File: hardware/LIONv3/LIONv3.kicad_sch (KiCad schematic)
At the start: 31 parts, among them SW1 RESET, SW2 BOOT, U14 HC-1_25-2PWT, U15 HC-1_25-2PWT, U19 HC-1_25-2PWT, U2 TYPE-C_16PIN_2MD(073), U21 USBLC6-2SC6, U3 ESP32-C6-MINI-1-N4, U4 TMP112AIDRLR, U9 HC-1_25-2PWT

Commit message: feat(hardware): add pre-review schematic
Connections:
- net +4.4V renamed +4.69V
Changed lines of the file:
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@@
+	)
+	(symbol
+		(lib_id "power:+5V")
+		(at 113.03 166.37 0)
+		(unit 1)
+		(body_style 1)
+		(exclude_from_sim no)
+		(in_bom yes)
+		(on_board yes)
+		(in_pos_files yes)
+		(dnp no)
+		(fields_autoplaced yes)
+		(property "Reference" "#PWR046"
+			(at 113.03 170.18 0)
+			(hide yes)
+			(show_name no)
+			(do_not_autoplace no)
+			(effects
+				(font
+					(size 1.27 1.27)
+				)
+			)
+		)
+		(property "Value" "+4.69V"
+			(at 113.03 161.29 0)
+			(show_name no)
+			(do_not_autoplace yes)
+			(effects
+				(font
+					(size 1.27 1.27)
+				)
+			)
+		)
+		(property "Footprint" ""
+			(at 113.03 166.37 0)
+			(hide yes)
+			(show_name no)
+			(do_not_autoplace no)
+			(effects
+				(font
+					(size 1.27 1.27)
+				)
+			)
+		)
+		(property "Datasheet" ""
+			(at 113.03 166.37 0)
+			(hide yes)
+			(show_name no)
+			(do_not_autoplace no)
+			(effects
+				(font
+					(size 1.27 1.27)
+				)
+			)
+		)
+		(property "Description" "Power symbol creates a global label with name \"+5V\""
+			(at 113.03 166.37 0)
+			(hide yes)
+			(show_name no)
+			(do_not_autoplace no)
+			(effects
+				(font
+					(size 1.27 1.27)
+				)
+			)
+		)
+		(pin "1"
+		)
+		(instances
+			(project "LIONv3"
+				(path "/3cc9e06f-00d0-4bec-822f-2e156022ced4"
+					(reference "#PWR046")
+					(unit 1)
+				)
+			)
+		)
 	)
 	(symbol
@@
 					(unit 1)
 				)
-			)
-		)
-	)
-	(symbol
-		(lib_id "power:+5V")
-		(at 113.03 166.37 0)
-		(unit 1)
-		(body_style 1)
-		(exclude_from_sim no)
-		(in_bom yes)
-		(on_board yes)
-		(in_pos_files yes)
-		(dnp no)
-		(fields_autoplaced yes)
-		(property "Reference" "#PWR046"
-			(at 113.03 170.18 0)
-			(hide yes)
-			(show_name no)
-			(do_not_autoplace no)
-			(effects
-				(font
-					(size 1.27 1.27)
-				)
-			)
-		)
-		(property "Value" "+4.4V"
-			(at 113.03 161.29 0)
-			(show_name no)
-			(do_not_autoplace no)
-			(effects
-				(font
-					(size 1.27 1.27)
-				)
-			)
-		)
-		(property "Footprint" ""
-			(at 113.03 166.37 0)
-			(hide yes)
-			(show_name no)
-			(do_not_autoplace no)
-			(effects
-				(font
-					(size 1.27 1.27)
-				)
-			)
-		)
-		(property "Datasheet" ""
-			(at 113.03 166.37 0)
-			(hide yes)
-			(show_name no)
-			(do_not_autoplace no)
-			(effects
-				(font
-					(size 1.27 1.27)
-				)
-			)
-		)
-		(property "Description" "Power symbol creates a global label with name \"+5V\""
-			(at 113.03 166.37 0)
-			(hide yes)
-			(show_name no)
-			(do_not_autoplace no)
-			(effects
-				(font
-					(size 1.27 1.27)
-				)
-			)
-		)
-		(pin "1"
-		)
-		(instances
-			(project "LIONv3"
-				(path "/3cc9e06f-00d0-4bec-822f-2e156022ced4"
-					(reference "#PWR046")
-					(unit 1)
-				)

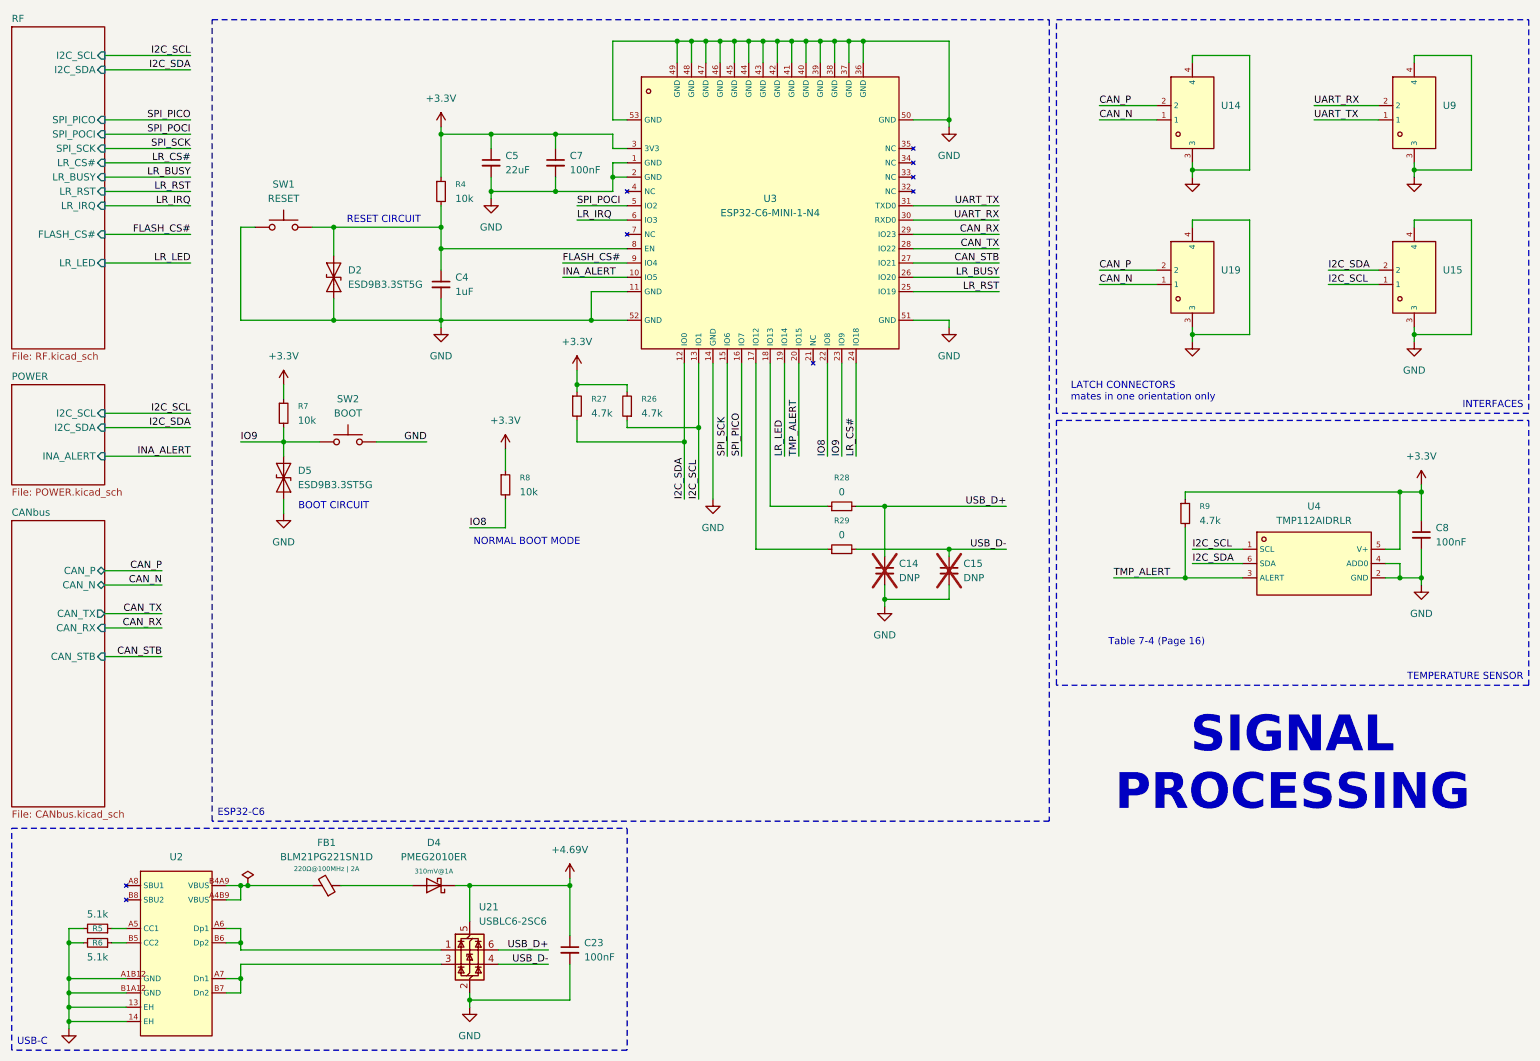
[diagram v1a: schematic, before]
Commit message: feat(hardware): add TestPoints
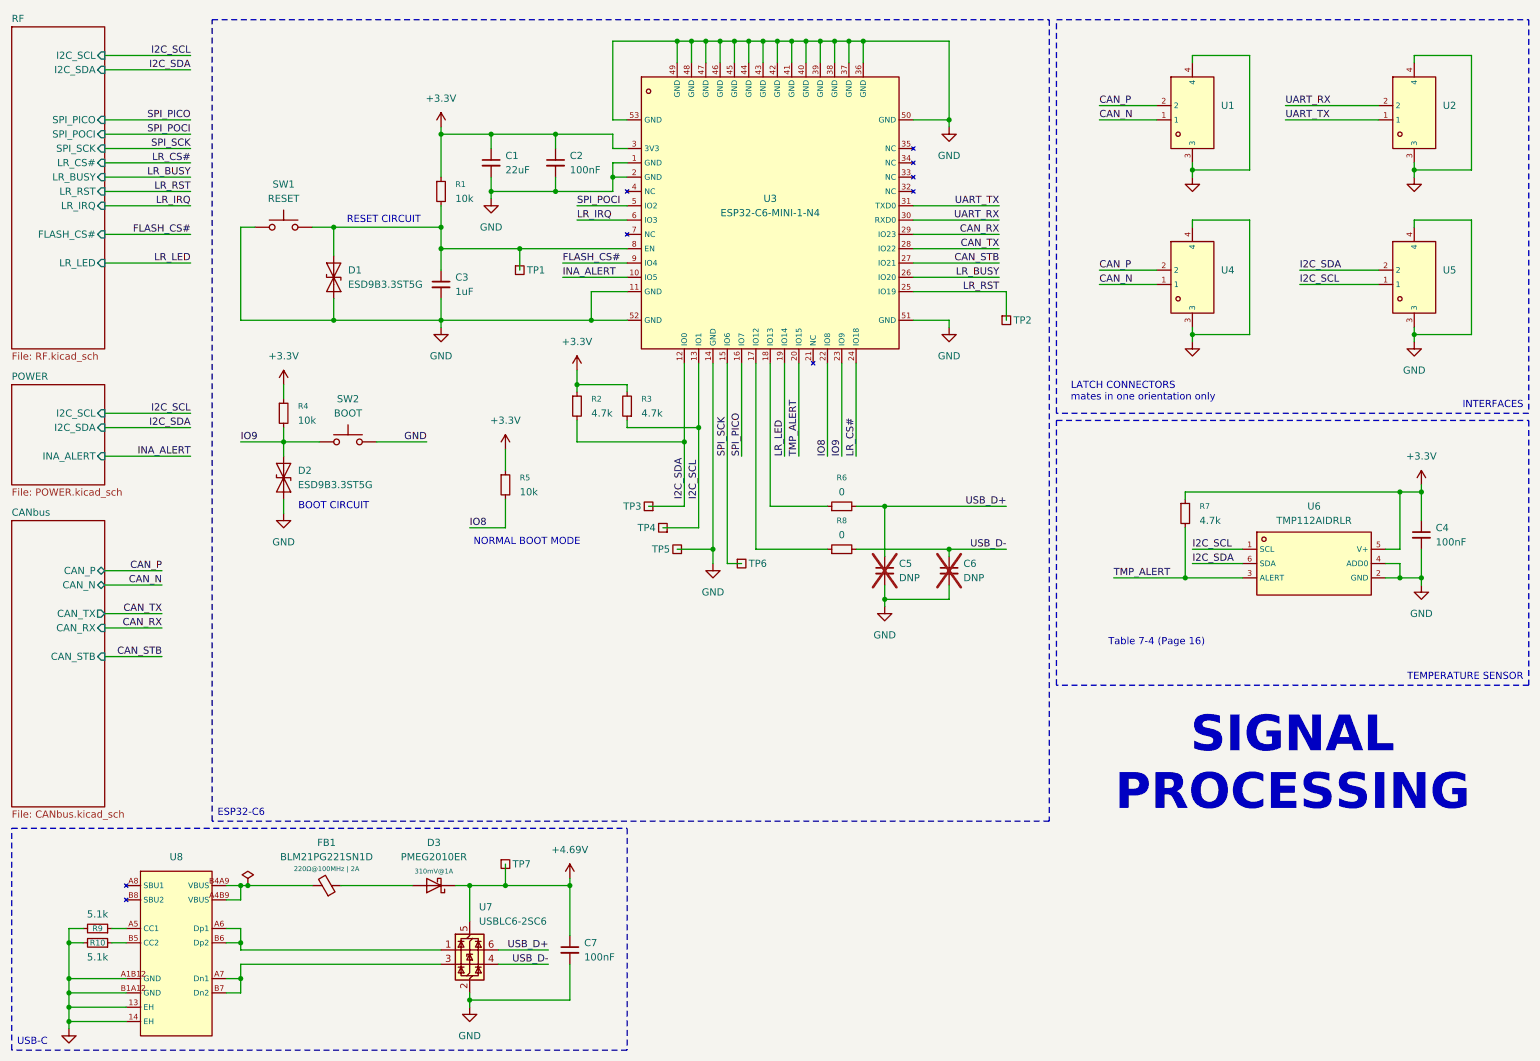
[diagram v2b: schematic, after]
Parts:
- added TP1, TP2, TP3, TP4, TP5, TP6, TP7: TestPoint_Square, TestPoint:TestPoint_Pad_D1.5mm, symbol Connector:TestPoint_Square
- renumbered C5 to C1, C7 to C2, C4 to C3, C8 to C4, C14 to C5, C15 to C6, C23 to C7, D2 to D1, D5 to D2, D4 to D3, R4 to R1, R6 to R10, R27 to R2, R26 to R3, R7 to R4, R8 to R5, R28 to R6, R9 to R7, R29 to R8, R5 to R9, U14 to U1, U9 to U2, U19 to U4, U15 to U5, U4 to U6, U21 to U7, U2 to U8
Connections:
- net +4.69V: now also TP7.1
- net GND: now also TP5.1
- net I2C_SCL: now also TP4.1
- net I2C_SDA: now also TP3.1
- net LR_RST: now also TP2.1
- net SPI_SCK: now also TP6.1
- net at C3.1, D1.2 (A2), R1.2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: now also TP1.1

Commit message: feat(hardware): start PCB design
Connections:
- net D+: now reaches U7.1 (I/O1), U8.A6 (Dp1), U8.B6 (Dp2)
- net D-: now reaches U7.3 (I/O2), U8.A7 (Dn1), U8.B7 (Dn2)
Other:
- moved on the sheet: SW1
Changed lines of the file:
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@@
 	(text "RESET CIRCUIT"
 		(exclude_from_sim no)
-		(at 80.01 49.53 0)
+		(at 80.01 50.8 0)
 		(effects
 			(font
@@
 	)
 	(junction
-		(at 90.17 50.8)
-		(diameter 0)
-		(color 0 0 0 0)
-	)
-	(junction
 		(at 110.49 34.29)
 		(diameter 0)
@@
 	)
 	(junction
+		(at 90.17 52.07)
+		(diameter 0)
+		(color 0 0 0 0)
+	)
+	(junction
 		(at 147.32 17.78)
 		(diameter 0)
@@
 	)
 	(junction
-		(at 71.12 50.8)
-		(diameter 0)
-		(color 0 0 0 0)
-	)
-	(junction
 		(at 262.89 69.85)
 		(diameter 0)
@@
 	)
 	(junction
-		(at 71.12 67.31)
+		(at 110.49 44.45)
 		(diameter 0)
 		(color 0 0 0 0)
 	)
 	(junction
-		(at 110.49 44.45)
+		(at 160.02 17.78)
 		(diameter 0)
 		(color 0 0 0 0)
 	)
 	(junction
-		(at 160.02 17.78)
+		(at 71.12 67.31)
 		(diameter 0)
 		(color 0 0 0 0)
@@
 	)
 	(junction
+		(at 71.12 52.07)
+		(diameter 0)
+		(color 0 0 0 0)
+	)
+	(junction
 		(at 168.91 100.33)
 		(diameter 0)
@@
 	(wire
 		(pts
-			(xy 90.17 46.99) (xy 90.17 50.8)
-		)
-		(stroke
-			(width 0)
-			(type default)
-		)
-	)
-	(wire
-		(pts
 			(xy 90.17 63.5) (xy 90.17 67.31)
 		)
@@
 	(wire
 		(pts
-			(xy 54.61 50.8) (xy 57.15 50.8)
+			(xy 54.61 52.07) (xy 57.15 52.07)
+		)
+		(stroke
+			(width 0)
+			(type default)
+		)
+	)
+	(wire
+		(pts
+			(xy 90.17 46.99) (xy 90.17 52.07)
 		)
 		(stroke
@@
 	(wire
 		(pts
-			(xy 30.48 111.76) (xy 40.64 111.76)
+			(xy 30.48 111.76) (xy 45.72 111.76)
 		)
 		(stroke
@@
 	(wire
 		(pts
-			(xy 30.48 127) (xy 40.64 127)
+			(xy 30.48 127) (xy 45.72 127)
 		)
 		(stroke
@@
 	(wire
 		(pts
-			(xy 54.61 50.8) (xy 54.61 67.31)
+			(xy 54.61 52.07) (xy 54.61 67.31)
 		)
 		(stroke
@@
 	(wire
 		(pts
+			(xy 90.17 52.07) (xy 90.17 54.61)
+		)
+		(stroke
+			(width 0)
+			(type default)
+		)
+	)
+	(wire
+		(pts
 			(xy 30.48 86.36) (xy 45.72 86.36)
 		)
@@
 	(wire
 		(pts
-			(xy 30.48 121.92) (xy 40.64 121.92)
+			(xy 30.48 121.92) (xy 45.72 121.92)
 		)
 		(stroke
@@
 	(wire
 		(pts
-			(xy 71.12 50.8) (xy 90.17 50.8)
+			(xy 71.12 52.07) (xy 90.17 52.07)
 		)
 		(stroke
@@
 	(wire
 		(pts
-			(xy 67.31 50.8) (xy 71.12 50.8)
+			(xy 67.31 52.07) (xy 71.12 52.07)
 		)
 		(stroke
@@
 	(wire
 		(pts
-			(xy 30.48 114.3) (xy 40.64 114.3)
+			(xy 30.48 114.3) (xy 45.72 114.3)
 		)
 		(stroke
@@
 	(wire
 		(pts
-			(xy 71.12 50.8) (xy 71.12 55.88)
-		)
-		(stroke
-			(width 0)
-			(type default)
-		)
-	)
-	(wire
-		(pts
 			(xy 158.75 107.95) (xy 146.05 107.95)
 		)
@@
 	(wire
 		(pts
-			(xy 90.17 50.8) (xy 90.17 54.61)
-		)
-		(stroke
-			(width 0)
-			(type default)
-		)
-	)
-	(wire
-		(pts
 			(xy 127 100.33) (xy 133.35 100.33)
 		)
@@
 	(wire
 		(pts
-			(xy 30.48 119.38) (xy 40.64 119.38)
+			(xy 30.48 119.38) (xy 45.72 119.38)
 		)
 		(stroke
@@
 	(wire
 		(pts
+			(xy 71.12 52.07) (xy 71.12 55.88)
+		)
+		(stroke
+			(width 0)
+			(type default)
+		)
+	)
+	(wire
+		(pts
 			(xy 114.3 88.9) (xy 114.3 85.09)
 		)
@@
 	)
 	(label "CAN_N"
-		(at 40.64 114.3 180)
+		(at 45.72 114.3 180)
 		(effects
 			(font
@@
 	)
 	(label "CAN_STB"
-		(at 40.64 127 180)
+		(at 45.72 127 180)
 		(effects
 			(font
@@
 		)
 	)
+	(label "D-"
+		(at 73.66 181.61 0)
+		(effects
+			(font
+				(size 1.27 1.27)
+			)
+			(justify left bottom)
+		)
+	)
 	(label "UART_TX"
 		(at 189.23 46.99 180)
@@
 	)
 	(label "CAN_TX"
-		(at 40.64 119.38 180)
+		(at 45.72 119.38 180)
 		(effects
 			(font
@@
 	)
 	(label "CAN_P"
-		(at 40.64 111.76 180)
+		(at 45.72 111.76 180)
 		(effects
 			(font
@@
 	)
 	(label "CAN_RX"
-		(at 40.64 121.92 180)
+		(at 45.72 121.92 180)
 		(effects
 			(font
@@
 		)
 	)
+	(label "D+"
+		(at 73.66 179.07 0)
+		(effects
+			(font
+				(size 1.27 1.27)
+			)
+			(justify left bottom)
+		)
+	)
 	(symbol
 		(lib_id "power:+5V")
@@
 	(symbol
 		(lib_id "Switch:SW_Push")
-		(at 62.23 50.8 0)
+		(at 62.23 52.07 0)
 		(unit 1)
 		(body_style 1)
@@
 		(fields_autoplaced yes)
 		(property "Reference" "SW1"
-			(at 62.23 43.18 0)
+			(at 62.23 44.45 0)
 			(show_name no)
 			(do_not_autoplace no)
@@
 		)
 		(property "Value" "RESET"
-			(at 62.23 45.72 0)
+			(at 62.23 46.99 0)
 			(show_name no)
 			(do_not_autoplace no)
@@
 		)
 		(property "Footprint" "LIONv3-Footprints:KEY-SMD_L3.9-W3.0-LS5.0"
-			(at 62.23 45.72 0)
+			(at 62.23 46.99 0)
 			(hide yes)
 			(show_name no)
@@
 		)
 		(property "Datasheet" ""
-			(at 62.23 45.72 0)
+			(at 62.23 46.99 0)
 			(hide yes)
 			(show_name no)
@@
 		)
 		(property "Description" "Push button switch, generic, two pins"
-			(at 62.23 50.8 0)
+			(at 62.23 52.07 0)
 			(hide yes)
 			(show_name no)
@@
 		)
 		(property "LCSC" "C5373431"
-			(at 62.23 50.8 0)
+			(at 62.23 52.07 0)
 			(hide yes)
 			(show_name no)

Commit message: feat(hardware): add board form-factor
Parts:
- removed U4: HC-1_25-2PWT, LIONv3-Footprints:CONN-SMD_2P-P1.25-HC-1.25-2PWT, symbol LIONv3-Symbols:HC-1_25-2PWT
- added H1, H2, H3: MountingHole_Pad, MountingHole:MountingHole_2.5mm_Pad, symbol Mechanical:MountingHole_Pad
- U3: footprint LIONv3-Footprints:WIFIM-SMD_61P-L16.6-W13.2-P0.80-ESP32-C6-MINI-1-N4 -> RF_Module:ESP32-C6-MINI-1
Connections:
- net GND: now also H1.1, H2.1, H3.1

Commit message: refactor(hardware): improve via fencing
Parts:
- H1, H2, H3: footprint MountingHole:MountingHole_2.5mm_Pad -> MountingHole:MountingHole_2.5mm
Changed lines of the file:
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@@
 			)
 		)
-		(property "Footprint" "MountingHole:MountingHole_2.5mm_Pad"
+		(property "Footprint" "MountingHole:MountingHole_2.5mm"
 			(at 208.28 62.23 0)
 			(hide yes)
@@
 			)
 		)
-		(property "Footprint" "MountingHole:MountingHole_2.5mm_Pad"
+		(property "Footprint" "MountingHole:MountingHole_2.5mm"
 			(at 217.17 62.23 0)
 			(hide yes)
@@
 			)
 		)
-		(property "Footprint" "MountingHole:MountingHole_2.5mm_Pad"
+		(property "Footprint" "MountingHole:MountingHole_2.5mm"
 			(at 226.06 62.23 0)
 			(hide yes)

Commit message: feat(hardware): add LED layout
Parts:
- H1, H2, H3: symbol Mechanical:MountingHole_Pad -> Mechanical:MountingHole
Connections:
- net GND: no longer H1.1, H2.1, H3.1
- net ESP_USB_D-: now reaches R8.1, U3.17 (IO12)
- net ESP_USB_D+: now reaches R6.1, U3.18 (IO13)
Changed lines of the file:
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@@
 	)
 	(junction
-		(at 217.17 66.04)
-		(diameter 0)
-		(color 0 0 0 0)
-	)
-	(junction
 		(at 223.52 40.64)
 		(diameter 0)
@@
 	)
 	(junction
-		(at 208.28 66.04)
-		(diameter 0)
-		(color 0 0 0 0)
-	)
-	(junction
 		(at 260.35 113.03)
 		(diameter 0)
@@
 	(wire
 		(pts
-			(xy 217.17 66.04) (xy 217.17 64.77)
-		)
-		(stroke
-			(width 0)
-			(type default)
-		)
-	)
-	(wire
-		(pts
 			(xy 223.52 40.64) (xy 233.68 40.64)
 		)
@@
 	(wire
 		(pts
-			(xy 208.28 64.77) (xy 208.28 66.04)
-		)
-		(stroke
-			(width 0)
-			(type default)
-		)
-	)
-	(wire
-		(pts
 			(xy 264.16 96.52) (xy 264.16 97.79)
 		)
@@
 	(wire
 		(pts
-			(xy 217.17 66.04) (xy 226.06 66.04)
-		)
-		(stroke
-			(width 0)
-			(type default)
-		)
-	)
-	(wire
-		(pts
 			(xy 30.48 86.36) (xy 45.72 86.36)
 		)
@@
 	(wire
 		(pts
-			(xy 208.28 66.04) (xy 208.28 67.31)
-		)
-		(stroke
-			(width 0)
-			(type default)
-		)
-	)
-	(wire
-		(pts
 			(xy 168.91 116.84) (xy 180.34 116.84)
 		)
@@
 	(wire
 		(pts
-			(xy 208.28 66.04) (xy 217.17 66.04)
-		)
-		(stroke
-			(width 0)
-			(type default)
-		)
-	)
-	(wire
-		(pts
 			(xy 34.29 184.15) (xy 24.13 184.15)
 		)
@@
 	(wire
 		(pts
-			(xy 226.06 66.04) (xy 226.06 64.77)
-		)
-		(stroke
-			(width 0)
-			(type default)
-		)
-	)
-	(wire
-		(pts
 			(xy 262.89 40.64) (xy 273.05 40.64)
 		)
@@
 		)
 	)
+	(label "ESP_USB_D+"
+		(at 148.59 91.44 90)
+		(effects
+			(font
+				(size 1.27 1.27)
+			)
+			(justify left bottom)
+		)
+	)
 	(label "D-"
 		(at 73.66 181.61 0)
@@
 		)
 	)
+	(label "ESP_USB_D-"
+		(at 146.05 91.44 90)
+		(effects
+			(font
+				(size 1.27 1.27)
+			)
+			(justify left bottom)
+		)
+	)
 	(label "IO9"
 		(at 54.61 88.9 0)
@@
 	)
 	(symbol
-		(lib_id "Mechanical:MountingHole_Pad")
+		(lib_id "Mechanical:MountingHole")
 		(at 208.28 62.23 0)
 		(unit 1)
@@
 		(fields_autoplaced yes)
 		(property "Reference" "H1"
-			(at 210.82 60.9599 0)
+			(at 210.82 62.2299 0)
 			(show_name no)
 			(do_not_autoplace no)
@@
 			)
 		)
-		(property "Description" "Mounting Hole with connection"
+		(property "Description" "Mounting Hole without connection"
 			(at 208.28 62.23 0)
 			(hide yes)
@@
 			)
 		)
-		(pin "1"
-		)
 		(instances
 			(project "LIONv3"
@@
 	)
 	(symbol
-		(lib_id "Mechanical:MountingHole_Pad")
+		(lib_id "Mechanical:MountingHole")
 		(at 217.17 62.23 0)
 		(unit 1)
@@
 		(fields_autoplaced yes)
 		(property "Reference" "H2"
-			(at 219.71 60.9599 0)
+			(at 219.71 62.2299 0)
 			(show_name no)
 			(do_not_autoplace no)
@@
 			)
 		)
-		(property "Description" "Mounting Hole with connection"
+		(property "Description" "Mounting Hole without connection"
 			(at 217.17 62.23 0)
 			(hide yes)
@@
 			)
 		)
-		(pin "1"
-		)
 		(instances
 			(project "LIONv3"
@@
 	)
 	(symbol
-		(lib_id "Mechanical:MountingHole_Pad")
+		(lib_id "Mechanical:MountingHole")
 		(at 226.06 62.23 0)
 		(unit 1)
@@
 		(fields_autoplaced yes)
 		(property "Reference" "H3"
-			(at 228.6 60.9599 0)
+			(at 228.6 62.2299 0)
 			(show_name no)
 			(do_not_autoplace no)
@@
 			)
 		)
-		(property "Description" "Mounting Hole with connection"
+		(property "Description" "Mounting Hole without connection"
 			(at 226.06 62.23 0)
 			(hide yes)
@@
 			)
 		)
-		(pin "1"
-		)
 		(instances
 			(project "LIONv3"
@@
 					(unit 1)
 				)
-			)
-		)
-	)
-	(symbol
-		(lib_id "power:GND")
-		(at 208.28 67.31 0)
-		(unit 1)
-		(body_style 1)
-		(exclude_from_sim no)
-		(in_bom yes)
-		(on_board yes)
-		(in_pos_files yes)
-		(dnp no)
-		(fields_autoplaced yes)
-		(property "Reference" "#PWR08"
-			(at 208.28 73.66 0)
-			(hide yes)
-			(show_name no)
-			(do_not_autoplace no)
-			(effects
-				(font
-					(size 1.27 1.27)
-				)
-			)
-		)
-		(property "Value" "GND"
-			(at 208.28 72.39 0)
-			(show_name no)
-			(do_not_autoplace no)
-			(effects
-				(font
-					(size 1.27 1.27)
-				)
-			)
-		)
-		(property "Footprint" ""
-			(at 208.28 67.31 0)
-			(hide yes)
-			(show_name no)
-			(do_not_autoplace no)
-			(effects
-				(font
-					(size 1.27 1.27)
-				)
-			)
-		)
-		(property "Datasheet" ""
-			(at 208.28 67.31 0)
-			(hide yes)
-			(show_name no)
-			(do_not_autoplace no)
-			(effects
-				(font
-					(size 1.27 1.27)
-				)
-			)
-		)
-		(property "Description" "Power symbol creates a global label with name \"GND\" , ground"
-			(at 208.28 67.31 0)
-			(hide yes)
-			(show_name no)
-			(do_not_autoplace no)
-			(effects
-				(font
-					(size 1.27 1.27)
-				)
-			)
-		)
-		(pin "1"
-		)
-		(instances
-			(project "LIONv3"
-				(path "/3cc9e06f-00d0-4bec-822f-2e156022ced4"
-					(reference "#PWR08")
-					(unit 1)
-				)

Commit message: feat(hardware): improve PCB layout
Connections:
- net CAN_RX: now also U3.19 (IO14); no longer U3.29 (IO23)
- net CAN_STB: now also U3.24 (IO18); no longer U3.27 (IO21)
- net CAN_TX: now also U3.20 (IO15); no longer U3.28 (IO22)
- net LR_BUSY: now also U3.27 (IO21); no longer U3.26 (IO20)
- net LR_CS#: now also U3.28 (IO22); no longer U3.24 (IO18)
- net LR_IRQ: now also U3.26 (IO20); no longer U3.6 (IO3)
- net LR_LED: now also TP6.1, U3.15 (IO6); no longer U3.19 (IO14)
- net SPI_PICO: now also U3.30 (RXD0); no longer U3.16 (IO7)
- net SPI_POCI: now also U3.31 (TXD0); no longer U3.5 (IO2)
- net SPI_SCK: now also U3.29 (IO23); no longer TP6.1, U3.15 (IO6)
- net TMP_ALERT: now also U3.16 (IO7); no longer U3.20 (IO15)
- net UART_RX: now also U3.5 (IO2); no longer U3.30 (RXD0)
- net UART_TX: now also U3.6 (IO3); no longer U3.31 (TXD0)
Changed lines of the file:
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@@
 		)
 	)
-	(label "LR_BUSY"
+	(label "LR_IRQ"
 		(at 189.23 59.69 180)
 		(effects
@@
 		)
 	)
-	(label "LR_IRQ"
+	(label "UART_TX"
 		(at 114.3 49.53 0)
 		(effects
@@
 		)
 	)
-	(label "UART_RX"
+	(label "SPI_PICO"
 		(at 189.23 49.53 180)
 		(effects
@@
 		)
 	)
-	(label "UART_TX"
+	(label "SPI_POCI"
 		(at 189.23 46.99 180)
 		(effects
@@
 		)
 	)
-	(label "CAN_TX"
+	(label "LR_CS#"
 		(at 189.23 54.61 180)
 		(effects
@@
 		)
 	)
-	(label "CAN_RX"
+	(label "SPI_SCK"
 		(at 189.23 52.07 180)
 		(effects
@@
 		)
 	)
-	(label "SPI_POCI"
+	(label "UART_RX"
 		(at 114.3 46.99 0)
 		(effects
@@
 		)
 	)
-	(label "SPI_SCK"
+	(label "LR_LED"
 		(at 140.97 91.44 90)
 		(effects
@@
 		)
 	)
-	(label "TMP_ALERT"
+	(label "CAN_TX"
 		(at 153.67 91.44 90)
 		(effects
@@
 		)
 	)
-	(label "LR_LED"
+	(label "CAN_RX"
 		(at 151.13 91.44 90)
 		(effects
@@
 		)
 	)
-	(label "LR_CS#"
+	(label "CAN_STB"
 		(at 163.83 91.44 90)
 		(effects
@@
 		)
 	)
-	(label "CAN_STB"
+	(label "LR_BUSY"
 		(at 189.23 57.15 180)
 		(effects
@@
 		)
 	)
-	(label "SPI_PICO"
+	(label "TMP_ALERT"
 		(at 143.51 91.44 90)
 		(effects
